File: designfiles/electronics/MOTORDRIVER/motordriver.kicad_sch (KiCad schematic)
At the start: 0 parts

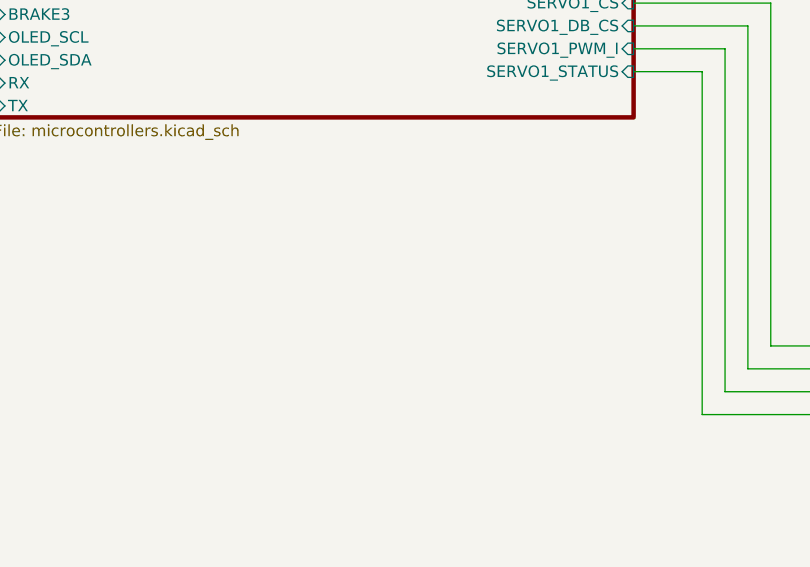
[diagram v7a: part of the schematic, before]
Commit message: layout rework, better ground plane
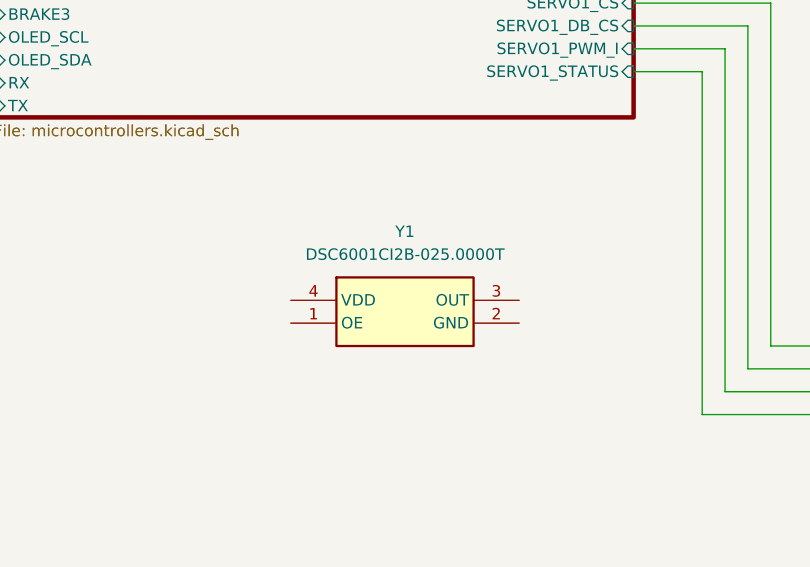
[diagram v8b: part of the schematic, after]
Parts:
- added Y1: DSC6001CI2B-025.0000T, DSC6001CI2B0250000T, symbol DSC6001CI2B-025_0000T:DSC6001CI2B-025.0000T
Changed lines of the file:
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@@
+		)
+	)
+	(symbol
+		(lib_id "DSC6001CI2B-025_0000T:DSC6001CI2B-025.0000T")
+		(at 105.41 132.08 0)
+		(unit 1)
+		(exclude_from_sim no)
+		(in_bom yes)
+		(on_board yes)
+		(dnp no)
+		(fields_autoplaced yes)
+		(property "Reference" "Y1"
+			(at 118.11 124.46 0)
+			(effects
+				(font
+					(size 1.27 1.27)
+				)
+			)
+		)
+		(property "Value" "DSC6001CI2B-025.0000T"
+			(at 118.11 127 0)
+			(effects
+				(font
+					(size 1.27 1.27)
+				)
+			)
+		)
+		(property "Footprint" "DSC6001CI2B0250000T"
+			(at 127 227 0)
+			(effects
+				(font
+					(size 1.27 1.27)
+				)
+				(justify left top)
+				(hide yes)
+			)
+		)
+		(property "Datasheet" "https://ww1.microchip.com/downloads/aemDocuments/documents/TCG/ProductDocuments/DataSheets/DSC60xxB-Ultra-Small-Ultra-Low-Power-MEMS-Oscillator-DS20006133.pdf"
+			(at 127 327 0)
+			(effects
+				(font
+					(size 1.27 1.27)
+				)
+				(justify left top)
+				(hide yes)
+			)
+		)
+		(property "Description" "Standard Clock Oscillators MEMS OSC, LVCMOS, 25MHz, 25PPM, 1.8-3.3V, -40 to 85C, 3.2 x 2.5mm"
+			(at 105.41 132.08 0)
+			(effects
+				(font
+					(size 1.27 1.27)
+				)
+				(hide yes)
+			)
+		)
+		(property "Height" "0.9"
+			(at 127 527 0)
+			(effects
+				(font
+					(size 1.27 1.27)
+				)
+				(justify left top)
+				(hide yes)
+			)
+		)
+		(property "Mouser Part Number" "579-1CI2B-025.0000T"
+			(at 127 627 0)
+			(effects
+				(font
+					(size 1.27 1.27)
+				)
+				(justify left top)
+				(hide yes)
+			)
+		)
+		(property "Mouser Price/Stock" "https://www.mouser.co.uk/ProductDetail/Microchip-Technology/DSC6001CI2B-025.0000T?qs=jRuttqqUwMT3Lnl3VzC%2FgA%3D%3D"
+			(at 127 727 0)
+			(effects
+				(font
+					(size 1.27 1.27)
+				)
+				(justify left top)
+				(hide yes)
+			)
+		)
+		(property "Manufacturer_Name" "Microchip"
+			(at 127 827 0)
+			(effects
+				(font
+					(size 1.27 1.27)
+				)
+				(justify left top)
+				(hide yes)
+			)
+		)
+		(property "Manufacturer_Part_Number" "DSC6001CI2B-025.0000T"
+			(at 127 927 0)
+			(effects
+				(font
+					(size 1.27 1.27)
+				)
+				(justify left top)
+				(hide yes)
+			)
+		)
+		(pin "2"
+		)
+		(pin "4"
+		)
+		(pin "1"
+		)
+		(pin "3"
+		)
+		(instances
+			(project ""
+				(path "/c7634e88-16d1-45ec-9aac-9c841e03cf6d"
+					(reference "Y1")
+					(unit 1)
+				)
+			)
 		)
 	)
